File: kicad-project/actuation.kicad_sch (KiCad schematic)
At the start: 34 parts, among them J10 Motor 2, J9 Motor 1, Q10 SI2300DS, Q11 SI2300DS, Q12 SI2300DS, Q13 SI2300DS, Q6 SI2300DS, Q7 SI2300DS, Q8 SI2300DS, Q9 SI2300DS

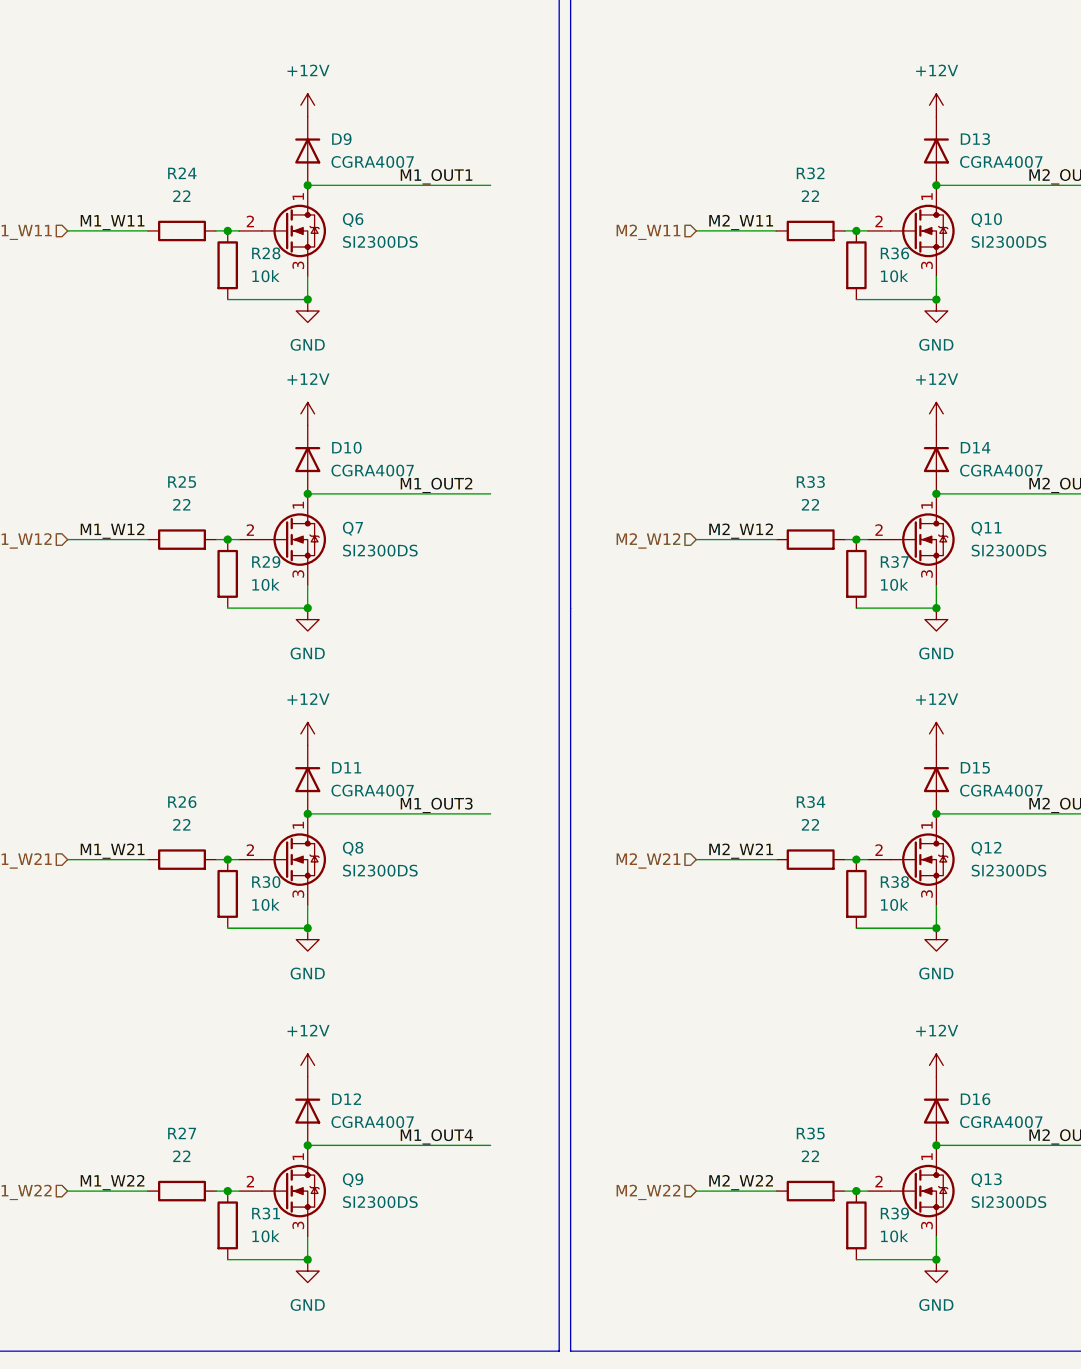
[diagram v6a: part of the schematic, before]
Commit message: hw: add mounting holes
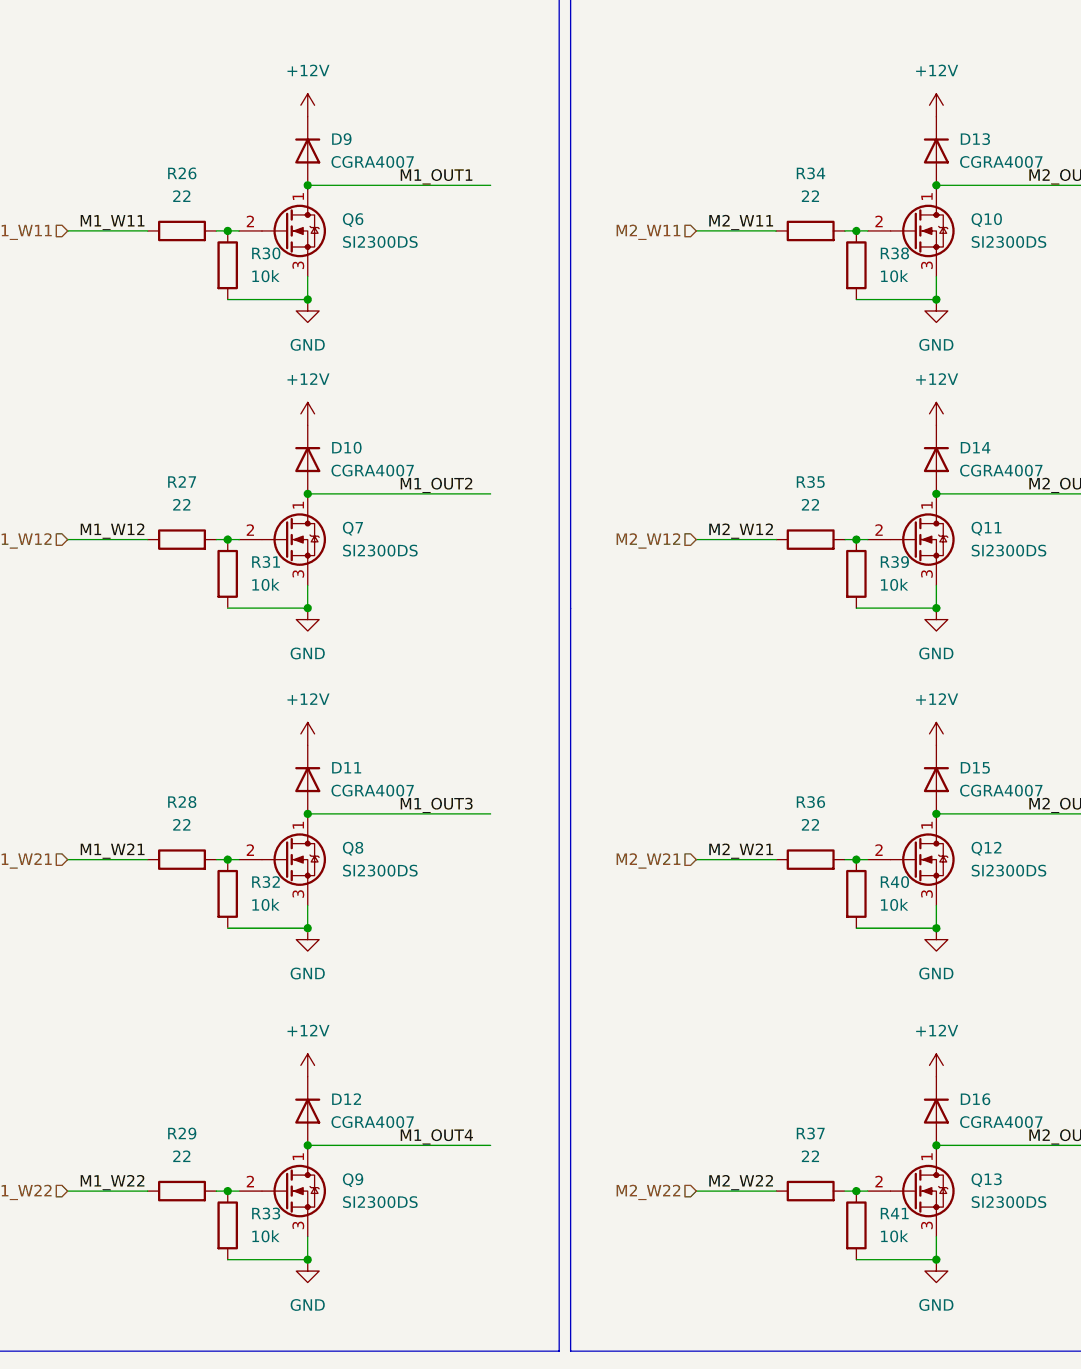
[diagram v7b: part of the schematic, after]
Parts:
- renumbered R24 to R26, R25 to R27, R26 to R28, R27 to R29, R28 to R30, R29 to R31, R30 to R32, R31 to R33, R32 to R34, R33 to R35, R34 to R36, R35 to R37, R36 to R38, R37 to R39, R38 to R40, R39 to R41
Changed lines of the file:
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@@
   (symbol (lib_id "Device:R") (at 115.57 163.83 0) (unit 1)
     (in_bom yes) (on_board yes) (fields_autoplaced)
-    (property "Reference" "R39" (id 0) (at 118.11 162.5599 0)
+    (property "Reference" "R41" (id 0) (at 118.11 162.5599 0)
       (effects (font (size 1.27 1.27)) (justify left))
     )
@@
   (symbol (lib_id "Device:R") (at 115.57 127 0) (unit 1)
     (in_bom yes) (on_board yes) (fields_autoplaced)
-    (property "Reference" "R38" (id 0) (at 118.11 125.7299 0)
+    (property "Reference" "R40" (id 0) (at 118.11 125.7299 0)
       (effects (font (size 1.27 1.27)) (justify left))
     )
@@
   (symbol (lib_id "Device:R") (at 40.64 123.19 90) (unit 1)
     (in_bom yes) (on_board yes) (fields_autoplaced)
-    (property "Reference" "R26" (id 0) (at 40.64 116.84 90))
+    (property "Reference" "R28" (id 0) (at 40.64 116.84 90))
     (property "Value" "22" (id 1) (at 40.64 119.38 90))
     (property "Footprint" "Resistor_SMD:R_0603_1608Metric" (id 2) (at 40.64 124.968 90)
@@
   (symbol (lib_id "Device:R") (at 40.64 87.63 90) (unit 1)
     (in_bom yes) (on_board yes) (fields_autoplaced)
-    (property "Reference" "R25" (id 0) (at 40.64 81.28 90))
+    (property "Reference" "R27" (id 0) (at 40.64 81.28 90))
     (property "Value" "22" (id 1) (at 40.64 83.82 90))
     (property "Footprint" "Resistor_SMD:R_0603_1608Metric" (id 2) (at 40.64 89.408 90)
@@
   (symbol (lib_id "Device:R") (at 45.72 91.44 0) (unit 1)
     (in_bom yes) (on_board yes) (fields_autoplaced)
-    (property "Reference" "R29" (id 0) (at 48.26 90.1699 0)
+    (property "Reference" "R31" (id 0) (at 48.26 90.1699 0)
       (effects (font (size 1.27 1.27)) (justify left))
     )
@@
   (symbol (lib_id "Device:R") (at 110.49 53.34 90) (unit 1)
     (in_bom yes) (on_board yes) (fields_autoplaced)
-    (property "Reference" "R32" (id 0) (at 110.49 46.99 90))
+    (property "Reference" "R34" (id 0) (at 110.49 46.99 90))
     (property "Value" "22" (id 1) (at 110.49 49.53 90))
     (property "Footprint" "Resistor_SMD:R_0603_1608Metric" (id 2) (at 110.49 55.118 90)
@@
   (symbol (lib_id "Device:R") (at 115.57 57.15 0) (unit 1)
     (in_bom yes) (on_board yes) (fields_autoplaced)
-    (property "Reference" "R36" (id 0) (at 118.11 55.8799 0)
+    (property "Reference" "R38" (id 0) (at 118.11 55.8799 0)
       (effects (font (size 1.27 1.27)) (justify left))
     )
@@
   (symbol (lib_id "Device:R") (at 115.57 91.44 0) (unit 1)
     (in_bom yes) (on_board yes) (fields_autoplaced)
-    (property "Reference" "R37" (id 0) (at 118.11 90.1699 0)
+    (property "Reference" "R39" (id 0) (at 118.11 90.1699 0)
       (effects (font (size 1.27 1.27)) (justify left))
     )
@@
   (symbol (lib_id "Device:R") (at 110.49 160.02 90) (unit 1)
     (in_bom yes) (on_board yes) (fields_autoplaced)
-    (property "Reference" "R35" (id 0) (at 110.49 153.67 90))
+    (property "Reference" "R37" (id 0) (at 110.49 153.67 90))
     (property "Value" "22" (id 1) (at 110.49 156.21 90))
     (property "Footprint" "Resistor_SMD:R_0603_1608Metric" (id 2) (at 110.49 161.798 90)
@@
   (symbol (lib_id "Device:R") (at 40.64 160.02 90) (unit 1)
     (in_bom yes) (on_board yes) (fields_autoplaced)
-    (property "Reference" "R27" (id 0) (at 40.64 153.67 90))
+    (property "Reference" "R29" (id 0) (at 40.64 153.67 90))
     (property "Value" "22" (id 1) (at 40.64 156.21 90))
     (property "Footprint" "Resistor_SMD:R_0603_1608Metric" (id 2) (at 40.64 161.798 90)
@@
   (symbol (lib_id "Device:R") (at 45.72 127 0) (unit 1)
     (in_bom yes) (on_board yes) (fields_autoplaced)
-    (property "Reference" "R30" (id 0) (at 48.26 125.7299 0)
+    (property "Reference" "R32" (id 0) (at 48.26 125.7299 0)
       (effects (font (size 1.27 1.27)) (justify left))
     )
@@
   (symbol (lib_id "Device:R") (at 45.72 57.15 0) (unit 1)
     (in_bom yes) (on_board yes) (fields_autoplaced)
-    (property "Reference" "R28" (id 0) (at 48.26 55.8799 0)
+    (property "Reference" "R30" (id 0) (at 48.26 55.8799 0)
       (effects (font (size 1.27 1.27)) (justify left))
     )
@@
   (symbol (lib_id "Device:R") (at 110.49 87.63 90) (unit 1)
     (in_bom yes) (on_board yes) (fields_autoplaced)
-    (property "Reference" "R33" (id 0) (at 110.49 81.28 90))
+    (property "Reference" "R35" (id 0) (at 110.49 81.28 90))
     (property "Value" "22" (id 1) (at 110.49 83.82 90))
     (property "Footprint" "Resistor_SMD:R_0603_1608Metric" (id 2) (at 110.49 89.408 90)
@@
   (symbol (lib_id "Device:R") (at 110.49 123.19 90) (unit 1)
     (in_bom yes) (on_board yes) (fields_autoplaced)
-    (property "Reference" "R34" (id 0) (at 110.49 116.84 90))
+    (property "Reference" "R36" (id 0) (at 110.49 116.84 90))
     (property "Value" "22" (id 1) (at 110.49 119.38 90))
     (property "Footprint" "Resistor_SMD:R_0603_1608Metric" (id 2) (at 110.49 124.968 90)
@@
   (symbol (lib_id "Device:R") (at 45.72 163.83 0) (unit 1)
     (in_bom yes) (on_board yes) (fields_autoplaced)
-    (property "Reference" "R31" (id 0) (at 48.26 162.5599 0)
+    (property "Reference" "R33" (id 0) (at 48.26 162.5599 0)
       (effects (font (size 1.27 1.27)) (justify left))
     )
@@
   (symbol (lib_id "Device:R") (at 40.64 53.34 90) (unit 1)
     (in_bom yes) (on_board yes) (fields_autoplaced)
-    (property "Reference" "R24" (id 0) (at 40.64 46.99 90))
+    (property "Reference" "R26" (id 0) (at 40.64 46.99 90))
     (property "Value" "22" (id 1) (at 40.64 49.53 90))
     (property "Footprint" "Resistor_SMD:R_0603_1608Metric" (id 2) (at 40.64 55.118 90)
